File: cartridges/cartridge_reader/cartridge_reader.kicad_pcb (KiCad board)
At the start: 2 copper layers, 68.6 x 53.3 mm, 3 parts, among them J1 P2000T_cartridge_edge, U1 4040

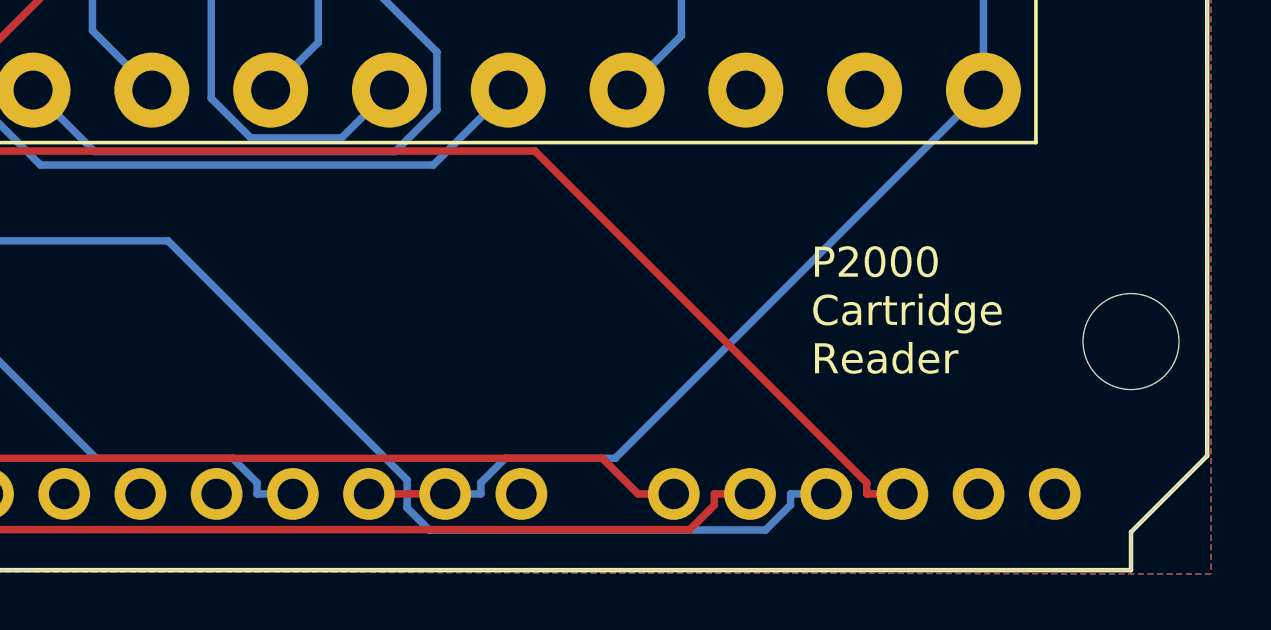
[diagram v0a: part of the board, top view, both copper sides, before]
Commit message: Making small adjustments to lay-out
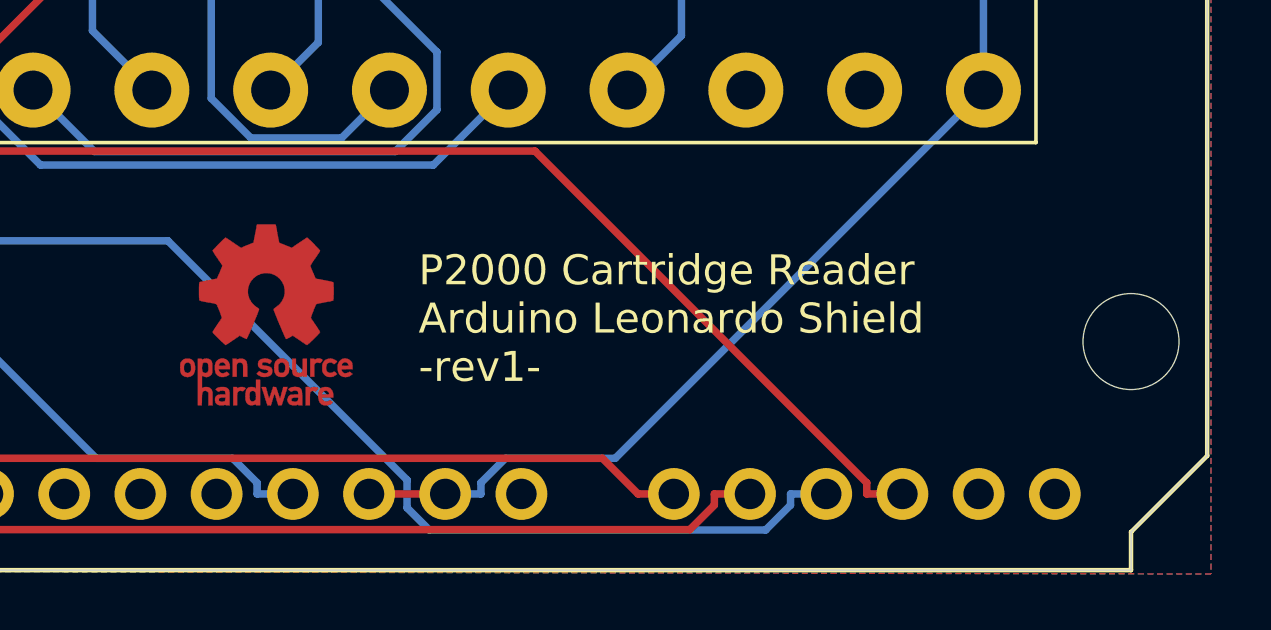
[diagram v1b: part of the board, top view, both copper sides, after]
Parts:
- added REF**: OSHW-Logo_5.7x6mm_Copper, Symbol:OSHW-Logo_5.7x6mm_Copper, F.Cu at (66.0, 70.2)
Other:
- board text added: "P2000 Cartridge Reader Arduino Leonardo Shield -rev1-"
- board text removed: "P2000 Cartridge Reader"
